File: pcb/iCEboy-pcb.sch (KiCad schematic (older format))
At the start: 64 parts, among them J1 dmg-card, J2 PROG_PORT, Q1 2N7002K, U1 TC74LCXR163245FT, U2 TC74LCXR163245FT, U3 ICE40UP5K-SG48ITR, U4 TPS79901DDCR, U5 TPS79901DDCR, U6 W25Q80DVSSIG, X1 SIT2001B

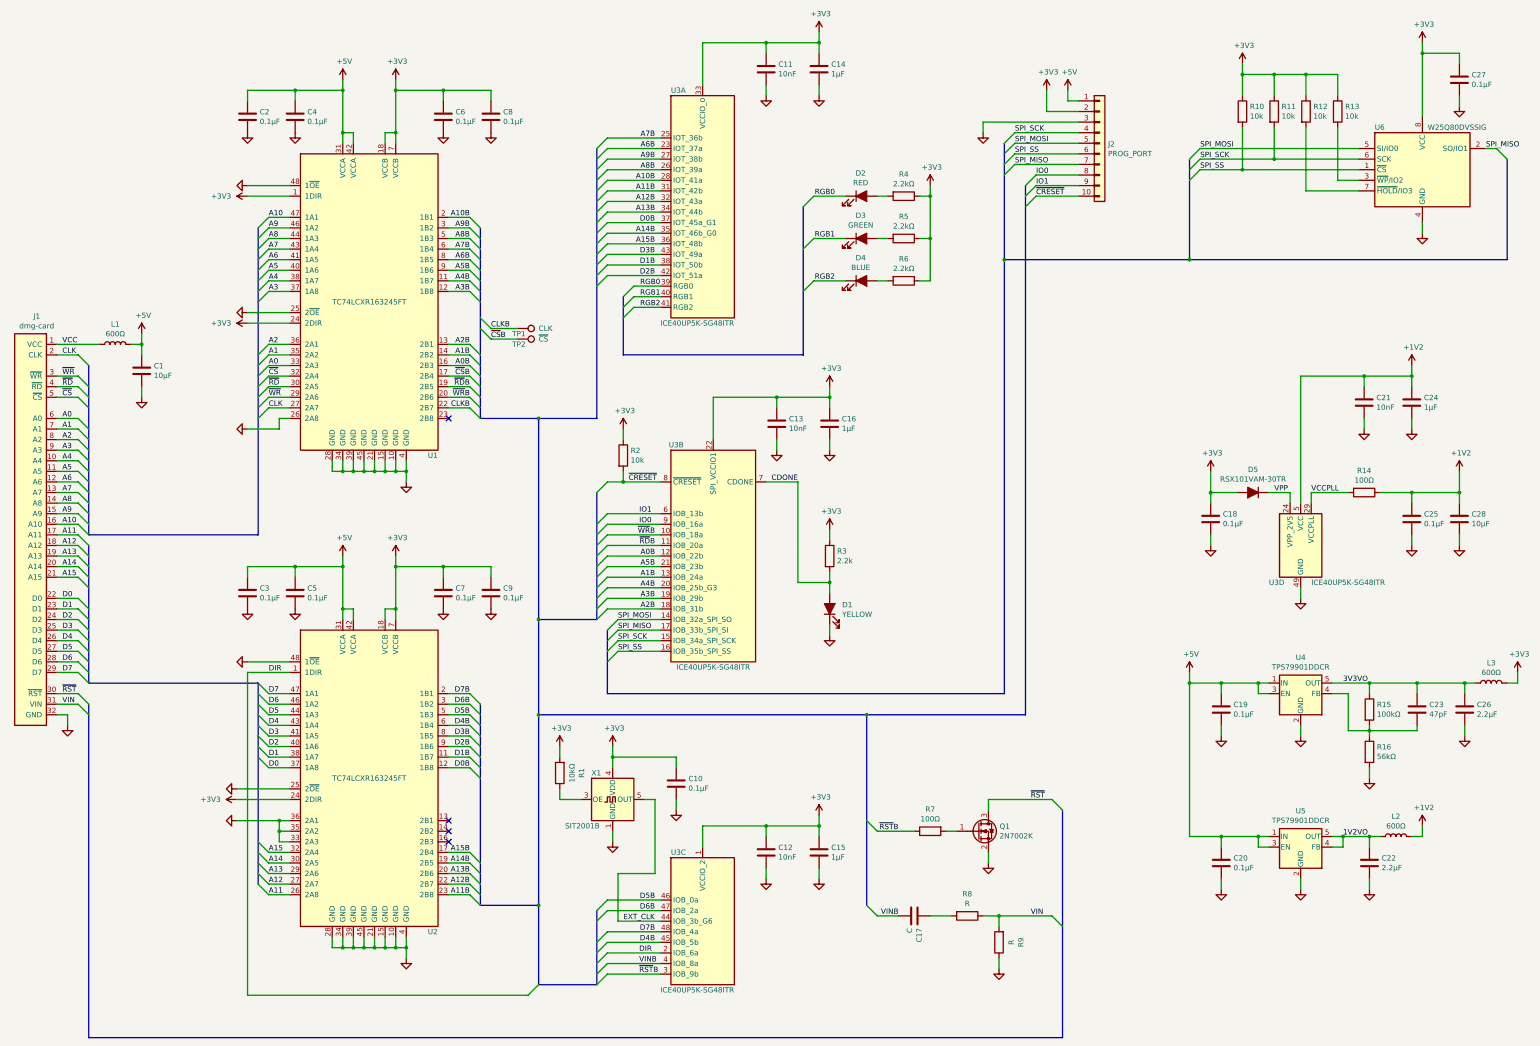
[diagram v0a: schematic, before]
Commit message: modify value fields
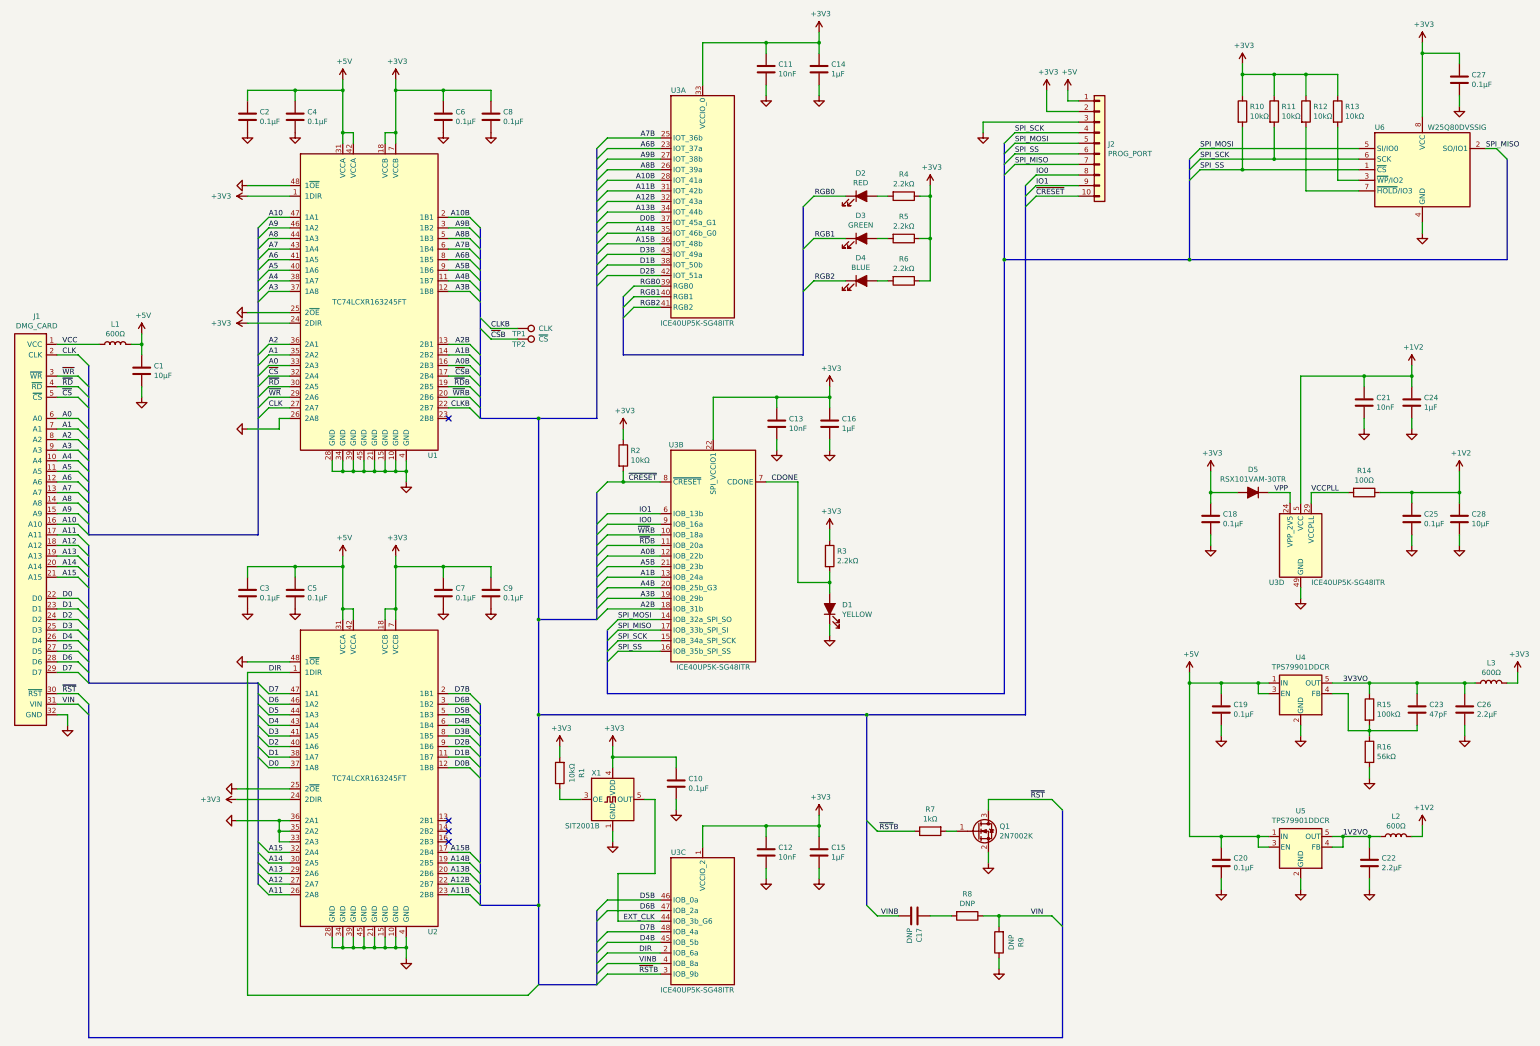
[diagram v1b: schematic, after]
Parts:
- C17: value C -> DNP
- J1: value dmg-card -> DMG_CARD
- R10, R11, R12, R13, R2: value 10k -> 10kΩ
- R3: value 2.2k -> 2.2kΩ
- R7: value 100Ω -> 1kΩ
- R8, R9: value R -> DNP
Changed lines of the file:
@@
 P 1550 5900
 F 0 "J1" H 1608 7915 50  0000 C CNN
-F 1 "dmg-card" H 1608 7824 50  0000 C CNN
+F 1 "DMG_CARD" H 1608 7824 50  0000 C CNN
 F 2 "dmg-card:dmg-card" H 1550 4000 50  0001 C CNN
 F 3 "" H 1800 7250 50  0001 C CNN
@@
 P 9100 6150
 F 0 "R3" H 9170 6196 50  0000 L CNN
-F 1 "2.2k" H 9170 6105 50  0000 L CNN
+F 1 "2.2kΩ" H 9170 6105 50  0000 L CNN
 F 2 "Resistor_SMD:R_0603_1608Metric" V 9030 6150 50  0001 C CNN
 F 3 "~" H 9100 6150 50  0001 C CNN
@@
 P 13000 1950
 F 0 "R10" H 13070 1996 50  0000 L CNN
-F 1 "10k" H 13070 1905 50  0000 L CNN
+F 1 "10kΩ" H 13070 1905 50  0000 L CNN
 F 2 "Resistor_SMD:R_0603_1608Metric" V 12930 1950 50  0001 C CNN
 F 3 "~" H 13000 1950 50  0001 C CNN
@@
 P 13300 1950
 F 0 "R11" H 13370 1996 50  0000 L CNN
-F 1 "10k" H 13370 1905 50  0000 L CNN
+F 1 "10kΩ" H 13370 1905 50  0000 L CNN
 F 2 "Resistor_SMD:R_0603_1608Metric" V 13230 1950 50  0001 C CNN
 F 3 "~" H 13300 1950 50  0001 C CNN
@@
 P 13600 1950
 F 0 "R12" H 13670 1996 50  0000 L CNN
-F 1 "10k" H 13670 1905 50  0000 L CNN
+F 1 "10kΩ" H 13670 1905 50  0000 L CNN
 F 2 "Resistor_SMD:R_0603_1608Metric" V 13530 1950 50  0001 C CNN
 F 3 "~" H 13600 1950 50  0001 C CNN
@@
 P 13900 1950
 F 0 "R13" H 13970 1996 50  0000 L CNN
-F 1 "10k" H 13970 1905 50  0000 L CNN
+F 1 "10kΩ" H 13970 1905 50  0000 L CNN
 F 2 "Resistor_SMD:R_0603_1608Metric" V 13830 1950 50  0001 C CNN
 F 3 "~" H 13900 1950 50  0001 C CNN
@@
 P 10050 8750
 F 0 "R7" V 9843 8750 50  0000 C CNN
-F 1 "100Ω" V 9934 8750 50  0000 C CNN
+F 1 "1kΩ" V 9934 8750 50  0000 C CNN
 F 2 "Resistor_SMD:R_0603_1608Metric" V 9980 8750 50  0001 C CNN
 F 3 "~" H 10050 8750 50  0001 C CNN
@@
 P 7150 5200
 F 0 "R2" H 7220 5246 50  0000 L CNN
-F 1 "10k" H 7220 5155 50  0000 L CNN
+F 1 "10kΩ" H 7220 5155 50  0000 L CNN
 F 2 "Resistor_SMD:R_0603_1608Metric" V 7080 5200 50  0001 C CNN
 F 3 "~" H 7150 5200 50  0001 C CNN
@@
 P 10400 9550
 F 0 "R8" V 10193 9550 50  0000 C CNN
-F 1 "R" V 10284 9550 50  0000 C CNN
+F 1 "DNP" V 10284 9550 50  0000 C CNN
 F 2 "Resistor_SMD:R_0603_1608Metric" V 10330 9550 50  0001 C CNN
 F 3 "~" H 10400 9550 50  0001 C CNN
@@
 P 9900 9550
 F 0 "C17" H 10015 9596 50  0000 L CNN
-F 1 "C" H 10015 9505 50  0000 L CNN
+F 1 "DNP" H 10015 9505 50  0000 L CNN
 F 2 "Capacitor_SMD:C_0603_1608Metric" H 9938 9400 50  0001 C CNN
 F 3 "~" H 9900 9550 50  0001 C CNN
@@
 P 10700 9800
 F 0 "R9" V 10493 9800 50  0000 C CNN
-F 1 "R" V 10584 9800 50  0000 C CNN
+F 1 "DNP" V 10584 9800 50  0000 C CNN
 F 2 "Resistor_SMD:R_0603_1608Metric" V 10630 9800 50  0001 C CNN
 F 3 "~" H 10700 9800 50  0001 C CNN

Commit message: modify decoup C value
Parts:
- C22, C26: value 2.2μF -> 4.7μF
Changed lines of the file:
@@
 P 15100 7600
 F 0 "C26" H 15215 7646 50  0000 L CNN
-F 1 "2.2μF" H 15215 7555 50  0000 L CNN
+F 1 "4.7μF" H 15215 7555 50  0000 L CNN
 F 2 "Capacitor_SMD:C_0603_1608Metric" H 15138 7450 50  0001 C CNN
 F 3 "~" H 15100 7600 50  0001 C CNN
@@
 P 14200 9050
 F 0 "C22" H 14315 9096 50  0000 L CNN
-F 1 "2.2μF" H 14315 9005 50  0000 L CNN
+F 1 "4.7μF" H 14315 9005 50  0000 L CNN
 F 2 "Capacitor_SMD:C_0603_1608Metric" H 14238 8900 50  0001 C CNN
 F 3 "~" H 14200 9050 50  0001 C CNN

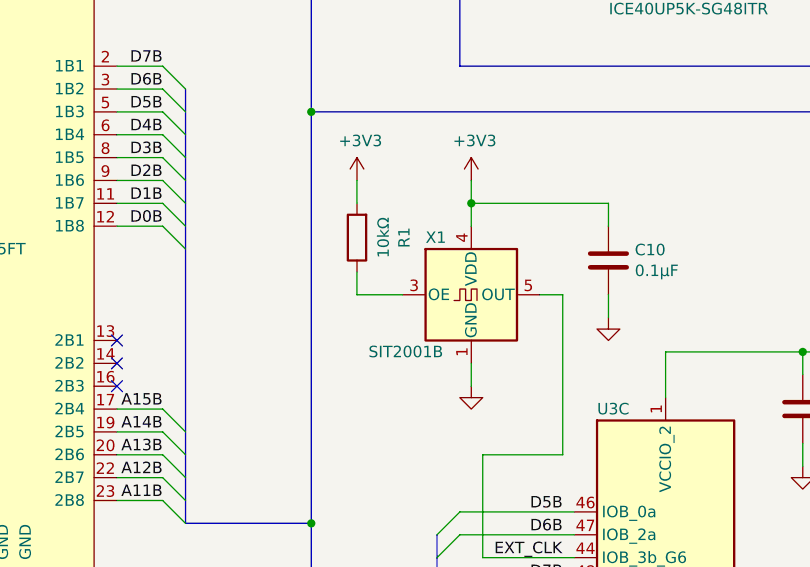
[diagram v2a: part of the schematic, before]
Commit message: change value of X1
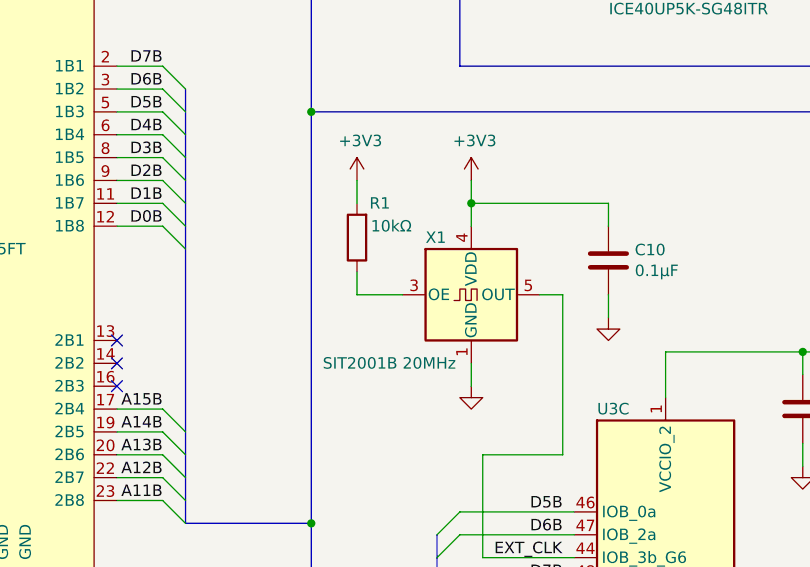
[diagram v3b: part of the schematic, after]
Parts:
- X1: value SIT2001B -> SIT2001B 20MHz
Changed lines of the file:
@@
 P 7050 8450
 F 0 "X1" H 6850 8700 50  0000 L CNN
-F 1 "SIT2001B" H 6600 8200 50  0000 L CNN
+F 1 "SIT2001B 20MHz" H 6400 8150 50  0000 L CNN
 F 2 "Package_TO_SOT_SMD:SOT-23-5" H 7500 8100 50  0001 C CNN
 F 3 "" H 6950 8450 50  0001 C CNN
@@
 U 1 1 600B707F
 P 6550 8200
-F 0 "R1" V 6343 8200 50  0000 C CNN
-F 1 "10kΩ" V 6434 8200 50  0000 C CNN
+F 0 "R1" H 6450 8050 50  0000 C CNN
+F 1 "10kΩ" H 6400 8150 50  0000 C CNN
 F 2 "Resistor_SMD:R_0603_1608Metric" V 6480 8200 50  0001 C CNN
 F 3 "~" H 6550 8200 50  0001 C CNN

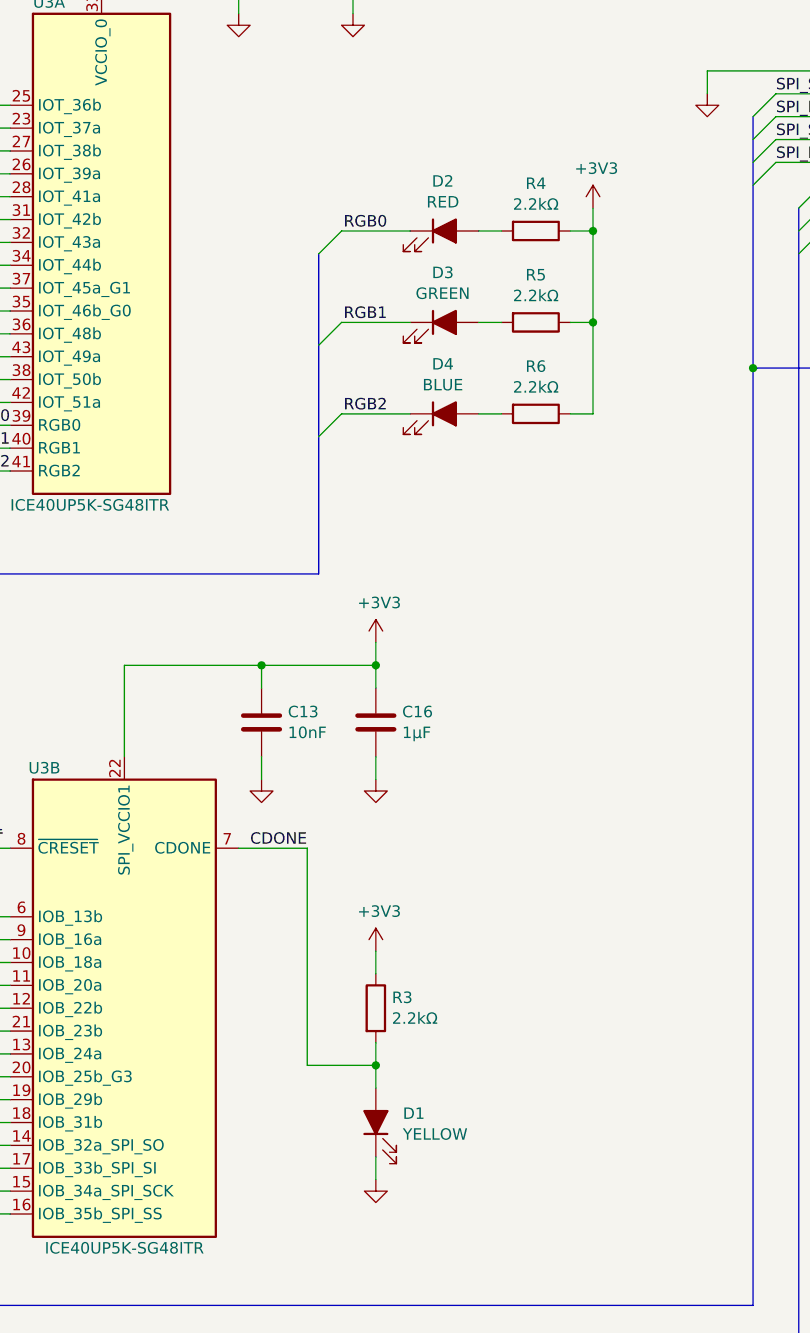
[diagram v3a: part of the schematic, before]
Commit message: update LED current limiting resistors
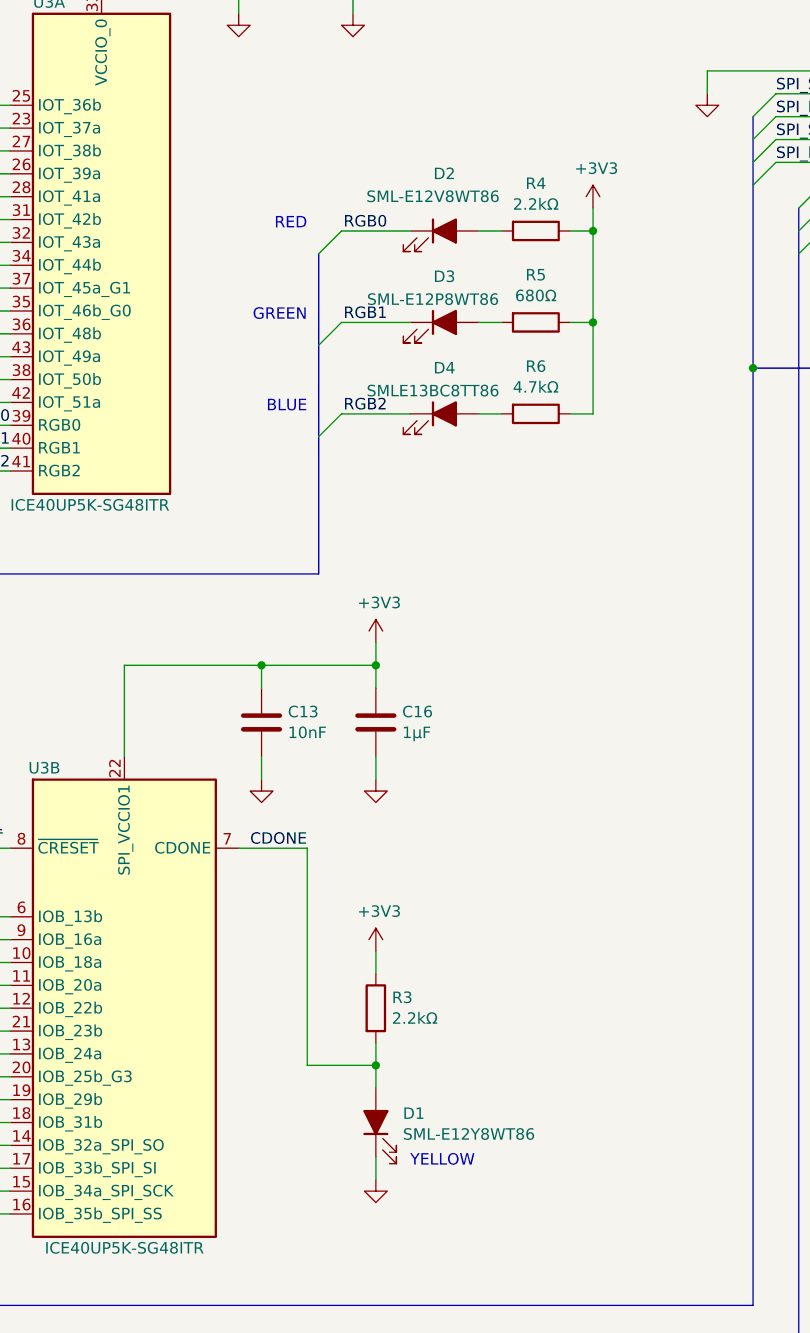
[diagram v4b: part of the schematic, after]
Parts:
- D1: value YELLOW -> SML-E12Y8WT86
- D2: value RED -> SML-E12V8WT86
- D3: value GREEN -> SML-E12P8WT86
- D4: value BLUE -> SMLE13BC8TT86
- R5: value 2.2kΩ -> 680Ω
- R6: value 2.2kΩ -> 4.7kΩ
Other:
- note added: "BLUE"
- note added: "GREEN"
- note added: "RED"
- note added: "YELLOW"
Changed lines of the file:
@@
 P 9100 6650
 F 0 "D1" V 9139 6532 50  0000 R CNN
-F 1 "YELLOW" V 9048 6532 50  0000 R CNN
+F 1 "SML-E12Y8WT86" V 9048 6532 50  0000 R CNN
 F 2 "LED_SMD:LED_0603_1608Metric_Castellated" H 9100 6650 50  0001 C CNN
 F 3 "~" H 9100 6650 50  0001 C CNN
@@
 U 1 1 5FE0310C
 P 9400 2750
-F 0 "D2" H 9393 2967 50  0000 C CNN
-F 1 "RED" H 9393 2876 50  0000 C CNN
+F 0 "D2" H 9400 3000 50  0000 C CNN
+F 1 "SML-E12V8WT86" H 9350 2900 50  0000 C CNN
 F 2 "LED_SMD:LED_0603_1608Metric_Castellated" H 9400 2750 50  0001 C CNN
 F 3 "~" H 9400 2750 50  0001 C CNN
@@
 P 9800 3150
 F 0 "R5" V 9593 3150 50  0000 C CNN
-F 1 "2.2kΩ" V 9684 3150 50  0000 C CNN
+F 1 "680Ω" V 9684 3150 50  0000 C CNN
 F 2 "Resistor_SMD:R_0603_1608Metric" V 9730 3150 50  0001 C CNN
 F 3 "~" H 9800 3150 50  0001 C CNN
@@
 U 1 1 5FE9BEF6
 P 9400 3150
-F 0 "D3" H 9393 3367 50  0000 C CNN
-F 1 "GREEN" H 9393 3276 50  0000 C CNN
+F 0 "D3" H 9400 3350 50  0000 C CNN
+F 1 "SML-E12P8WT86" H 9350 3250 50  0000 C CNN
 F 2 "LED_SMD:LED_0603_1608Metric_Castellated" H 9400 3150 50  0001 C CNN
 F 3 "~" H 9400 3150 50  0001 C CNN
@@
 P 9800 3550
 F 0 "R6" V 9593 3550 50  0000 C CNN
-F 1 "2.2kΩ" V 9684 3550 50  0000 C CNN
+F 1 "4.7kΩ" V 9684 3550 50  0000 C CNN
 F 2 "Resistor_SMD:R_0603_1608Metric" V 9730 3550 50  0001 C CNN
 F 3 "~" H 9800 3550 50  0001 C CNN
@@
 U 1 1 5FEDCA2F
 P 9400 3550
-F 0 "D4" H 9393 3767 50  0000 C CNN
-F 1 "BLUE" H 9393 3676 50  0000 C CNN
+F 0 "D4" H 9400 3750 50  0000 C CNN
+F 1 "SMLE13BC8TT86" H 9350 3650 50  0000 C CNN
 F 2 "LED_SMD:LED_0603_1608Metric_Castellated" H 9400 3550 50  0001 C CNN
 F 3 "~" H 9400 3550 50  0001 C CNN
@@
 Wire Bus Line
 	3700 7350 3700 9250
+Text Notes 8800 2750 2    50   ~ 0
+RED
+Text Notes 8800 3150 2    50   ~ 0
+GREEN
+Text Notes 8800 3550 2    50   ~ 0
+BLUE
+Text Notes 9250 6850 0    50   ~ 0
+YELLOW
 $EndSCHEMATC
